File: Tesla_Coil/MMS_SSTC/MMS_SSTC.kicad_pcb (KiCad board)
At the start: 2 copper layers, 100 x 79 mm, 54 parts, among them J1 Screw_Terminal_01x02, J2 Screw_Terminal_01x02, J3 Screw_Terminal_01x02, J4 Screw_Terminal_01x02, Q1 IRFP460APBF, U1 LM7812_TO220, U2 LM7805_TO220, U3 CD74HC14E, U4 UCC27524P, U5 NE555P

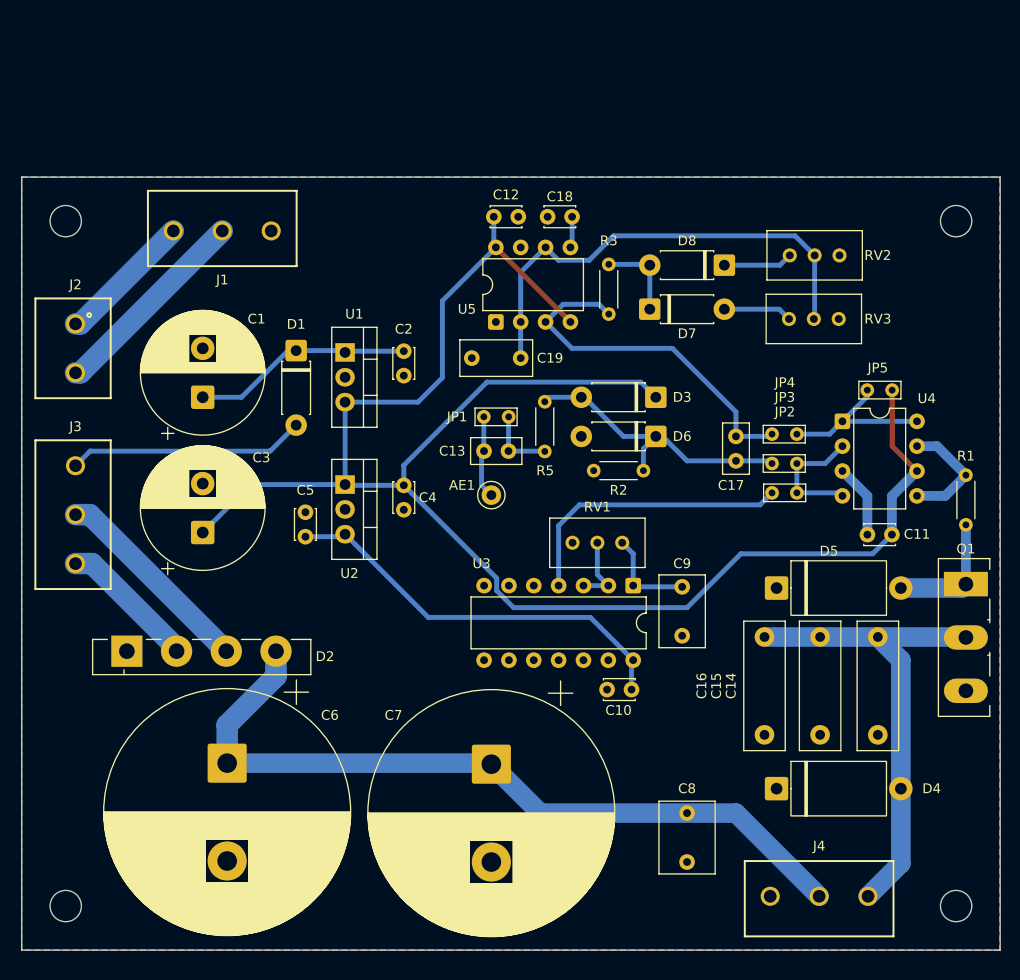
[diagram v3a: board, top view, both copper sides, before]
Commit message: Draft BOM for final SSTC design
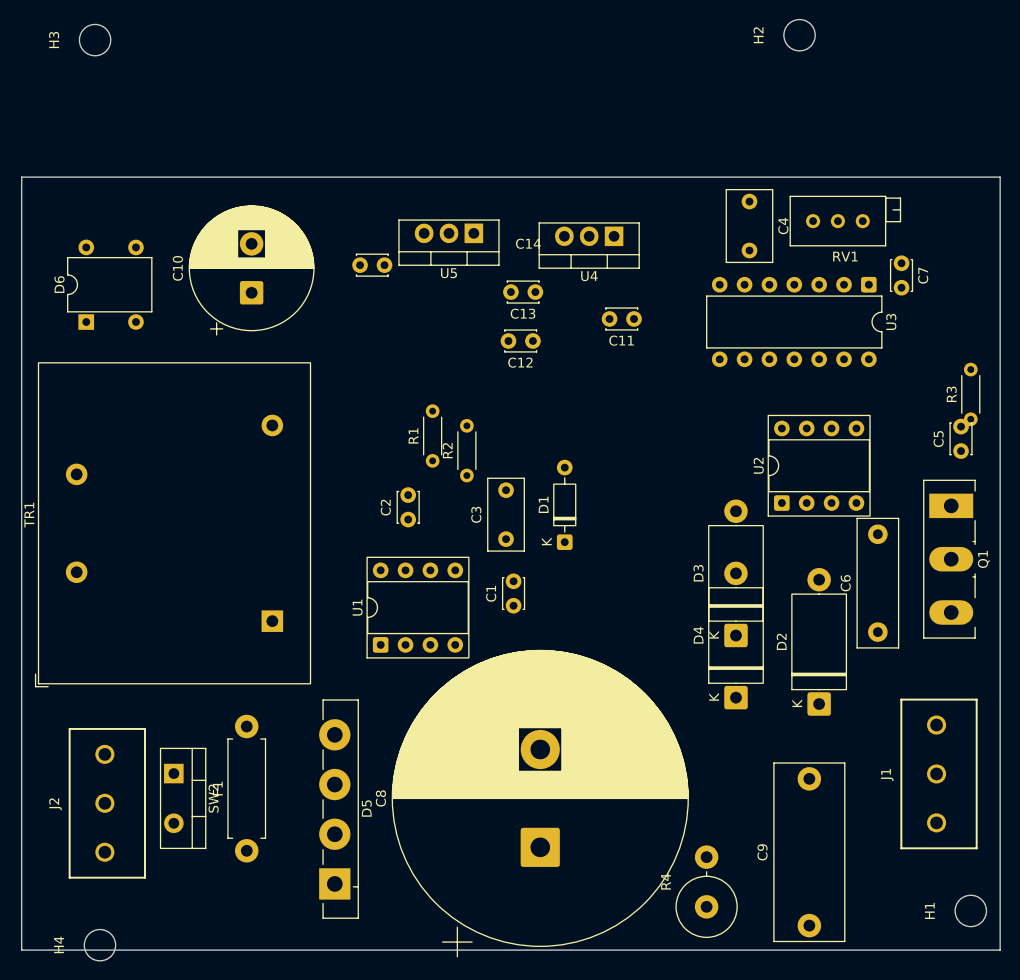
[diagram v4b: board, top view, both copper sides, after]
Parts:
- removed AE1: Antenna, TestPoint:TestPoint_Keystone_5000-5004_Miniature
- removed C15, C16: 1.5n, Capacitor_THT:C_Rect_L13.0mm_W4.0mm_P10.00mm_FKS3_FKP3_MKS4
- removed C17: 10n, Capacitor_THT:C_Disc_D5.0mm_W2.5mm_P2.50mm
- removed C18: 0.1u, Capacitor_THT:C_Disc_D3.0mm_W2.0mm_P2.50mm
- removed C19: 330n, Capacitor_THT:C_Rect_L7.2mm_W3.5mm_P5.00mm_FKS2_FKP2_MKS2_MKP2
- removed D7, D8: D_Small_Filled, Diode_THT:D_DO-41_SOD81_P7.62mm_Horizontal
- removed J3, J4: Screw_Terminal_01x02, locals:691137710003
- removed JP1, JP3, JP4: Jumper_2_Bridged, TestPoint:TestPoint_Bridge_Pitch2.54mm_Drill0.7mm
- removed JP2, JP5: Jumper_2_Open, TestPoint:TestPoint_Bridge_Pitch2.54mm_Drill0.7mm
- removed R5: 1k, Resistor_THT:R_Axial_DIN0204_L3.6mm_D1.6mm_P5.08mm_Horizontal
- removed RV2, RV3: R_Potentiometer_Trim_US, Potentiometer_THT:Potentiometer_Bourns_3296W_Vertical
- added F1: 4A, Resistor_THT:R_Axial_DIN0411_L9.9mm_D3.6mm_P12.70mm_Horizontal, F.Cu at (82.5, 97.8)
- added R4: 18k, Resistor_THT:R_Axial_DIN0617_L17.0mm_D6.0mm_P5.08mm_Vertical, F.Cu at (129.5, 103.6)
- added SW2: 70C, Package_TO_SOT_THT:TO-220-2_Vertical, F.Cu at (75.0, 90.0)
- added TR1: TRANSF1, locals:Transformer_Zettler_BV301S18028, F.Cu at (65.1, 74.4)
- C1: value 470u -> 0.1u; footprint Capacitor_THT:CP_Radial_D12.5mm_P5.00mm -> Capacitor_THT:C_Disc_D3.0mm_W2.0mm_P2.50mm
- C10: value 0.1u -> 470u; footprint Capacitor_THT:C_Disc_D3.0mm_W2.0mm_P2.50mm -> Capacitor_THT:CP_Radial_D12.5mm_P5.00mm
- C13: value 10n -> 0.1u; footprint Capacitor_THT:C_Disc_D5.0mm_W2.5mm_P2.50mm -> Capacitor_THT:C_Disc_D3.0mm_W2.0mm_P2.50mm
- C14: value 1.5n -> 0.1u; footprint Capacitor_THT:C_Rect_L13.0mm_W4.0mm_P10.00mm_FKS3_FKP3_MKS4 -> Capacitor_THT:C_Disc_D3.0mm_W2.0mm_P2.50mm
- C3: value 470u -> 330n; footprint Capacitor_THT:CP_Radial_D12.5mm_P5.00mm -> Capacitor_THT:C_Rect_L7.2mm_W3.5mm_P5.00mm_FKS2_FKP2_MKS2_MKP2
- C4: value 0.1u -> 470p; footprint Capacitor_THT:C_Disc_D3.0mm_W2.0mm_P2.50mm -> Capacitor_THT:C_Rect_L7.2mm_W4.5mm_P5.00mm_FKS2_FKP2_MKS2_MKP2
- C6: value 2200u -> 2.7n; footprint Capacitor_THT:CP_Radial_D25.0mm_P10.00mm_SnapIn -> Capacitor_THT:C_Rect_L13.0mm_W4.0mm_P10.00mm_FKS3_FKP3_MKS4
- C7: value 2200u -> 0.1u; footprint Capacitor_THT:CP_Radial_D25.0mm_P10.00mm_SnapIn -> Capacitor_THT:C_Disc_D3.0mm_W2.0mm_P2.50mm
- C8: value 0.68u -> 1500u; footprint Capacitor_THT:C_Rect_L7.2mm_W5.5mm_P5.00mm_FKS2_FKP2_MKS2_MKP2 -> Capacitor_THT:CP_Radial_D30.0mm_P10.00mm_SnapIn
- C9: value 470p -> 1u; footprint Capacitor_THT:C_Rect_L7.2mm_W4.5mm_P5.00mm_FKS2_FKP2_MKS2_MKP2 -> Capacitor_THT:C_Rect_L18.0mm_W7.0mm_P15.00mm_FKS3_FKP3
- D1: value D_Filled -> D_Small_Filled; footprint Diode_THT:D_DO-41_SOD81_P7.62mm_Horizontal -> Diode_THT:D_DO-35_SOD27_P7.62mm_Horizontal
- D2: value B125C2300-1500A -> 18V; footprint Diode_THT:Diode_Bridge_Vishay_GBU -> Diode_THT:D_DO-27_P12.70mm_Horizontal
- D3: value ~ -> 400V; footprint Diode_THT:D_DO-41_SOD81_P7.62mm_Horizontal -> Diode_THT:D_DO-27_P12.70mm_Horizontal
- D5: value 18V -> B125C2300-1500A; footprint Diode_THT:D_DO-27_P12.70mm_Horizontal -> Diode_THT:Diode_Bridge_Vishay_GBU
- D6: value ~ -> DB105; footprint Diode_THT:D_DO-41_SOD81_P7.62mm_Horizontal -> Diode_THT:Diode_Bridge_DIP-4_W7.62mm_P5.08mm
- J2: footprint locals:691137710002 -> locals:691137710003
- Q1: value IRFP460APBF -> FQA8N100C
- R1: value 1.5R -> 18k
- R2: value 220k -> 150k
- R3: value 1k -> 1.5R
- RV1: footprint Potentiometer_THT:Potentiometer_Bourns_3296W_Vertical -> Potentiometer_THT:Potentiometer_Bourns_3296X_Horizontal
- U1: value LM7812_TO220 -> NE555P; footprint Package_TO_SOT_THT:TO-220-3_Vertical -> Package_DIP:DIP-8_W7.62mm_Socket
- U2: value LM7805_TO220 -> UCC37322P; footprint Package_TO_SOT_THT:TO-220-3_Vertical -> Package_DIP:DIP-8_W7.62mm_Socket
- U4: value UCC27524P -> LM7812_TO220; footprint Package_DIP:DIP-8_W7.62mm -> Package_TO_SOT_THT:TO-220-3_Vertical
- U5: value NE555P -> LM7805_TO220; footprint Package_DIP:DIP-8_W7.62mm -> Package_TO_SOT_THT:TO-220-3_Vertical
- moved H3 124.8 mm to (67.0, 15.0), turned to 90 degrees
- moved J1 91.7 mm to (153.0, 90.0), turned to 90 degrees
- moved H2 77.4 mm to (139.0, 14.5), turned to 90 degrees
- moved D2 71.0 mm to (141.0, 82.8), turned to 90 degrees
- moved H1 70.5 mm to (156.5, 104.0), turned to 90 degrees
- moved C6 67.8 mm to (147.0, 75.5), turned to 90 degrees
- moved C5 67.6 mm to (155.5, 57.0)
- moved C7 66.2 mm to (149.4, 37.8)
- moved C14 63.1 mm to (96.6, 38.0), turned to 180 degrees
- moved D6 59.4 mm to (66.1, 43.8), turned to 90 degrees
- moved R1 54.9 mm to (101.5, 58.0)
- moved C10 54.4 mm to (83.0, 40.8), turned to 90 degrees
- moved D5 54.3 mm to (91.5, 101.2), turned to 90 degrees
- moved J2 46.6 mm to (68.0, 93.0), turned to 90 degrees
- moved C4 45.7 mm to (133.9, 31.5)
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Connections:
- C1 pad 1: Net-(D1-K) -> Net-(U1-CV)
- C1 pad 2: Earth -> GND
- C10 pad 1: Earth -> Net-(D6-+)
- C10 pad 2: +5V -> GND
- C11 pad 1: Earth -> Net-(D6-+)
- C11 pad 2: +12V -> GND
- C12 pad 2: Earth -> GND
- C13 pad 1: Net-(AE1-A) -> +12V
- C13 pad 2: Net-(JP1-B) -> GND
- C14 pad 1: Net-(D4-A2) -> +5V
- C14 pad 2: Earth -> GND
- C2 pad 1: Net-(D1-K) -> +12V
- C2 pad 2: Earth -> GND
- C3 pad 1: +12V -> Net-(U1-THR)
- C3 pad 2: Earth -> GND
- C4 pad 1: +12V -> Net-(U3-1A)
- C4 pad 2: Earth -> GND
- C5 pad 1: +5V -> GND
- C5 pad 2: Earth -> +12V
- C6 pad 1: +68V -> Net-(D3-A2)
- C6 pad 2: Earth -> GND
- C7 pad 1: +68V -> GND
- C7 pad 2: Earth -> +5V
- C8 pad 1: +68V -> +170V
- C8 pad 2: Earth -> GND
- C9 pad 1: Net-(U3-1A) -> +170V
- C9 pad 2: Earth -> GND
- D1 pad 2: 24VAC -> INTERRUPT_OUT
- D2 pad 1: Earth -> GND
- D2 pad 2: 0VAC -> Net-(D2-A2)
- D3 pad 1: +12V -> Net-(D3-A1)
- D3 pad 2: Net-(D3-A) -> Net-(D3-A2)
- D4 pad 1: Earth -> GND
- D4 pad 2: Net-(D4-A2) -> Net-(D3-A1)
- D5 pad 1: Earth -> GND
- D5 pad 2: Net-(D5-A2) -> AC_PROT
- D6 pad 1: Net-(D3-A) -> GND
- D6 pad 2: Earth -> Net-(D6-Pad2)
- J1 pad 1: HT -> Earth
- J1 pad 2: NEUT -> +170V
- J1 pad 3: Earth -> Net-(D3-A2)
- J2 pad 1: HT -> HT_SW
- Q1 pad 1: Net-(D5-A2) -> Net-(D2-A2)
- Q1 pad 2: Net-(D4-A2) -> Net-(D3-A2)
- Q1 pad 3: Earth -> GND
- R1 pad 1: Net-(D5-A2) -> Net-(D1-K)
- R1 pad 2: Net-(U4-OUTA) -> Net-(U1-THR)
- R2 pad 1: Earth -> Net-(U1-DIS)
- R2 pad 2: Net-(D3-A) -> Net-(U1-THR)
- R3 pad 1: INTERRUPT_OUT -> Net-(D2-A2)
- R3 pad 2: Net-(D7-A) -> Net-(U2-OUT)
- U1 pad 1: Net-(D1-K) -> GND
- U1 pad 2: Earth -> Net-(U1-THR)
- U1 pad 3: +12V -> INTERRUPT_OUT
- U2 pad 2: Earth -> OSC_OUT
- U2 pad 3: +5V -> INTERRUPT_OUT
- U3 pad 7: Earth -> GND
- U4 pad 1: Net-(JP4-B) -> Net-(D6-+)
- U4 pad 2: Net-(JP2-A) -> GND
- U4 pad 3: Earth -> +12V
- U5 pad 1: Earth -> +12V
- U5 pad 2: Net-(U5-THR) -> GND
- U5 pad 3: INTERRUPT_OUT -> +5V
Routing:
- net +12V: track 179.3 -> 0.00 mm
- net +68V: track 79.8 -> 0.00 mm
- net Net-(D4-A2): track 49.5 -> 0.00 mm
- net Net-(U5-THR): track 48.8 -> 0.00 mm
- net +5V: track 42.0 -> 0.00 mm
- net INTERRUPT_OUT: track 37.2 -> 0.00 mm
- net Net-(D3-A): track 30.7 -> 0.00 mm
- net OSC_OUT: track 29.3 -> 0.00 mm
- net 24VAC: track 24.4 -> 0.00 mm
- net Net-(D1-K): track 22.7 -> 0.00 mm
- net 48VAC: track 21.2 -> 0.00 mm
- net HT: track 21.0 -> 0.00 mm
- net Net-(JP4-B): track 17.1 -> 0.00 mm
- net 0VAC: track 14.2 -> 0.00 mm
- net NEUT: track 13.9 -> 0.00 mm
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- removed copper zone on B.Cu, net Earth
- removed copper zone on F.Cu, net Earth

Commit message: Rough layout on final SSTC PCB
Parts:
- removed C13, C14: 0.1u, Capacitor_THT:C_Disc_D3.0mm_W2.0mm_P2.50mm
- removed SW2: 70C, Package_TO_SOT_THT:TO-220-2_Vertical
- removed U5: LM7805_TO220, Package_TO_SOT_THT:TO-220-3_Vertical
- added D7: LED, LED_THT:LED_D3.0mm_Horizontal_O1.27mm_Z2.0mm, F.Cu at (90.7, 105.2)
- added JP1: SolderJumper_2_Open, Jumper:SolderJumper-2_P1.3mm_Open_RoundedPad1.0x1.5mm, F.Cu at (106.5, 47.2)
- added R5: 1.2k, Resistor_THT:R_Axial_DIN0204_L3.6mm_D1.6mm_P5.08mm_Horizontal, F.Cu at (97.5, 104.5)
- added R6: 1.8k, Resistor_THT:R_Axial_DIN0204_L3.6mm_D1.6mm_P5.08mm_Horizontal, F.Cu at (100.0, 49.5)
- added R7: 1.5k, Resistor_THT:R_Axial_DIN0204_L3.6mm_D1.6mm_P5.08mm_Horizontal, F.Cu at (103.5, 49.5)
- C8: value 1500u -> 570u
- R4: value 18k -> 8.2k
- RV1: value 10k -> 2.2k
- U3: footprint Package_DIP:DIP-14_W7.62mm -> locals:N14
- moved U3 32.8 mm to (113.9, 34.0), turned to 180 degrees
- moved D5 28.0 mm to (68.0, 86.0), turned to 0 degrees
- moved C7 26.4 mm to (124.0, 44.8)
- moved R4 20.6 mm to (109.1, 107.0), turned to 180 degrees
- moved C5 20.6 mm to (134.9, 57.0), turned to 180 degrees
- moved C9 19.1 mm to (126.0, 92.5), turned to -90 degrees
- moved H3 18.7 mm to (64.0, 33.5)
- moved H2 18.6 mm to (141.0, 33.0)
- moved D2 17.8 mm to (127.0, 71.8)
- moved U2 17.7 mm to (129.9, 46.2), turned to 0 degrees
- moved H1 17.6 mm to (140.0, 110.0)
- moved J1 16.2 mm to (138.0, 96.0), turned to -90 degrees
- moved RV1 16.0 mm to (126.0, 40.5), turned to -90 degrees
- moved C1 15.5 mm to (115.7, 58.4), turned to -90 degrees
- moved U4 15.5 mm to (104.5, 34.0)
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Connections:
- net +5V renamed Net-(JP1-A)
- F1 pad 2: Net-(SW2-A) -> AC_PROT
- R4 pad 2: GND -> Net-(D7-A)
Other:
- board size 100 x 79 mm -> 85 x 85.5 mm

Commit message: Commit progress on final SSTC board
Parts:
- removed R7: 1.5k, Resistor_THT:R_Axial_DIN0204_L3.6mm_D1.6mm_P5.08mm_Horizontal
- added D8: 5.6V, Diode_THT:D_DO-35_SOD27_P7.62mm_Horizontal, F.Cu at (114.0, 48.8)
- R6: value 1.8k -> 1k
- U3: footprint locals:N14 -> Package_DIP:DIP-14_W7.62mm_Socket
- moved TR1 27.1 mm to (85.5, 53.0), turned to -90 degrees
- moved C1 20.8 mm to (97.2, 68.0), turned to 0 degrees
- moved U3 18.1 mm to (124.6, 48.5)
- moved C9 15.3 mm to (129.0, 107.5), turned to 180 degrees
- moved C3 14.9 mm to (108.8, 57.2), turned to 0 degrees
- moved D1 12.8 mm to (114.3, 68.6), turned to 90 degrees
- moved R6 12.6 mm to (111.0, 43.5), turned to -90 degrees
- moved C5 12.2 mm to (142.0, 47.0)
- moved C11 10.4 mm to (98.5, 34.0), turned to 0 degrees
- moved U1 9.42 mm to (105.1, 57.5), turned to -90 degrees
- moved R1 9.01 mm to (108.6, 66.1), turned to 90 degrees
- moved C7 8.67 mm to (119.2, 52.0), turned to 180 degrees
- moved U4 7.84 mm to (98.5, 39.0), turned to 0 degrees
- moved D6 6.38 mm to (69.5, 36.4), turned to 0 degrees
- moved C2 5.91 mm to (97.7, 54.5), turned to 0 degrees
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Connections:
- net Net-(D2-A2) renamed /GATE
- C6 pad 1: Net-(D3-A2) -> /DRAIN
- D3 pad 2: Net-(D3-A2) -> /DRAIN
- J1 pad 1: Earth -> /DRAIN
- J1 pad 3: Net-(D3-A2) -> Earth
- Q1 pad 2: Net-(D3-A2) -> /DRAIN
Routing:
- net +12V: track 0.00 -> 102.1 mm
- net +170V: track 0.00 -> 93.5 mm
- net Earth: track 0.00 -> 65.7 mm
- net AC_PROT: track 0.00 -> 49.8 mm
- net NEUT: track 0.00 -> 41.1 mm
- net INTERRUPT_OUT: track 0.00 -> 35.7 mm
- net /DRAIN: track 0.00 -> 33.9 mm
- net Net-(D6-Pad2): track 0.00 -> 33.1 mm
- net Net-(U1-THR): track 0.00 -> 21.2 mm
- net Net-(D6-Pad3): track 0.00 -> 20.0 mm
- net Net-(U3-1A): track 0.00 -> 15.9 mm
- net OSC_OUT: track 0.00 -> 15.4 mm
- net Net-(D8-K): track 0.00 -> 14.7 mm
- net /GATE: track 0.00 -> 14.2 mm
- net HT_SW: track 0.00 -> 11.4 mm
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- added copper zone on B.Cu, net GND
- added copper zone on F.Cu, net GND

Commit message: route SSTC PCB and then find out critical problem yay
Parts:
- removed JP1: SolderJumper_2_Open, Jumper:SolderJumper-2_P1.3mm_Open_RoundedPad1.0x1.5mm
- F1: value 4A -> 4A 115VAC SLOW BLOW
- moved C7 20.0 mm to (122.3, 32.2)
- moved F1 17.3 mm to (67.0, 104.1), turned to 90 degrees
- moved C4 16.2 mm to (119.8, 47.0), turned to 180 degrees
- moved C9 15.9 mm to (124.6, 92.2), turned to 0 degrees
- moved J1 14.7 mm to (126.5, 101.6), turned to 0 degrees
- moved RV1 14.3 mm to (115.2, 40.6)
- moved D8 14.0 mm to (110.5, 35.2), turned to -90 degrees
- moved C11 12.5 mm to (102.0, 46.0), turned to 90 degrees
- moved U3 7.41 mm to (119.9, 42.8), turned to 90 degrees
- moved C12 6.93 mm to (102.0, 40.8), turned to 90 degrees
- moved U4 6.83 mm to (99.2, 45.8), turned to 90 degrees
- moved R6 4.08 mm to (107.5, 41.3), turned to 90 degrees
- moved C5 3.35 mm to (139.0, 45.5), turned to -90 degrees
- moved R5 2.60 mm to (93.0, 104.0), turned to 90 degrees
- moved C1 1.48 mm to (98.6, 67.5)
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- renumbered D7 to LED1
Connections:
- J1 pad 1: /DRAIN -> Earth
- J1 pad 3: Earth -> /DRAIN
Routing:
- net +170V: track 93.5 -> 70.1 mm
- net +12V: track 102.1 -> 80.3 mm
- net Net-(D6-+): track 11.4 -> 29.4 mm
- net Earth: track 65.7 -> 48.8 mm
- net /DRAIN: track 33.9 -> 49.6 mm
- net /GATE: track 14.2 -> 23.0 mm
- net Net-(U2-OUT): track 0.00 -> 8.05 mm
- net OSC_OUT: track 15.4 -> 9.06 mm
- net Net-(U3-1A): track 15.9 -> 9.90 mm
- net HT_SW: track 11.4 -> 7.78 mm
- net AC_PROT: track 49.8 -> 53.0 mm
- net NEUT: track 41.1 -> 38.3 mm
- net Net-(D8-K): track 14.7 -> 16.6 mm
- net Net-(U3-1Y): track 9.98 -> 11.7 mm
- net INTERRUPT_OUT: track 35.7 -> 35.0 mm
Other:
- board text added: "- ~ ~ +"
- board text added: "4A 115VAC SLOW BLOW"
- board text added: "EARTH (GREEN)"
- board text added: "LIVE (BLACK)"
- board text added: "NEUT (WHITE)"
- board text added: "PRIMARY"
- board text added: "SECONDARY"
- board text added: "|"

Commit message: FINISH THE DAMN THING
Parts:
- removed D8: 5.6V, Diode_THT:D_DO-35_SOD27_P7.62mm_Horizontal
- removed R6: 1k, Resistor_THT:R_Axial_DIN0204_L3.6mm_D1.6mm_P5.08mm_Horizontal
- added C13: 0.1u, Capacitor_THT:C_Disc_D3.0mm_W2.0mm_P2.50mm, F.Cu at (98.9, 39.0)
- added C14: 0.1u, Capacitor_THT:C_Disc_D3.0mm_W2.0mm_P2.50mm, F.Cu at (104.0, 39.0)
- added U5: LM7805_TO220, Package_TO_SOT_THT:TO-220-3_Vertical, F.Cu at (98.9, 36.0)
- F1: value 4A 115VAC SLOW BLOW -> 4A
- moved C12 8.94 mm to (104.0, 49.5), turned to 0 degrees
- moved C11 4.71 mm to (98.8, 49.5), turned to 0 degrees
- moved D1 1.27 mm to (116.5, 69.1)
- moved C2 1.18 mm to (98.5, 55.0)
- moved R2 1.12 mm to (113.0, 66.6)
- moved C1 1.08 mm to (98.2, 68.5)
- moved C3 1.08 mm to (109.8, 57.8)
- moved R1 1.08 mm to (109.6, 66.6)
- moved U1 1.08 mm to (106.1, 58.0)
- moved U4 0.94 mm to (99.0, 46.7), turned to 0 degrees
- moved RV1 0.89 mm to (115.4, 39.7)
- moved F1 0.75 mm to (67.0, 104.8)
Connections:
- net Net-(D8-K) renamed +5V
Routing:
- net GND: track 0.00 -> 9.00 mm
- net +5V: track 16.6 -> 22.7 mm
- net +12V: track 80.3 -> 74.7 mm
- net INTERRUPT_OUT: track 35.0 -> 36.6 mm
- net Net-(D1-K): track 6.74 -> 7.49 mm
- net Net-(U1-DIS): track 9.97 -> 10.7 mm
- net Net-(U1-THR): track 21.2 -> 21.9 mm
